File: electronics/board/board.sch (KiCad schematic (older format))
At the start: 50 parts

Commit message: Board update
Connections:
- net +5V: now also U?.24 (AVCC), U?.42 (AREF), U?.44 (AVCC)
- net at U?.1 (I1): now also U?.31 (PC6); no longer U?.18 (PD0)
- net at U?.2 (I2): now also U?.32 (PC7); no longer U?.19 (PD1)
- net at U?.3 (I3): now also U?.18 (PD0); no longer U?.20 (PD2)
- net at U?.4 (I4): now also U?.19 (PD1); no longer U?.21 (PD3)
- net at U?.5 (I5): now also U?.20 (PD2); no longer U?.25 (PD4)
- net at U?.6 (I6): now also U?.21 (PD3); no longer U?.22 (PD5)
- net at U?.7 (I7): now also U?.25 (PD4); no longer U?.26 (PD6)
- net at U?.8 (I8): now also U?.22 (PD5); no longer U?.27 (PD7)
- net at U?.1 (I1): now also U?.26 (PD6); no longer U?.41 (PF0)
- net at U?.2 (I2): now also U?.27 (PD7); no longer U?.40 (PF1)
- net at U?.3 (I3): now also U?.41 (PF0); no longer U?.39 (PF4)
- net at U?.4 (I4): now also U?.40 (PF1); no longer U?.38 (PF5)
- net at U?.5 (I5): now also U?.39 (PF4); no longer U?.37 (PF6)
- net at U?.6 (I6): now also U?.38 (PF5); no longer U?.36 (PF7)
- net at U?.7 (I7): now also U?.37 (PF6); no longer U?.31 (PC6)
- net at U?.8 (I8): now also U?.36 (PF7); no longer U?.32 (PC7)
- net at U?.2 (~RE): now also U?.3 (DE); no longer U?.29 (PB5)
- net at U?.30 (PB6): no longer U?.3 (DE)
- net at J?.1 (Pin_1), J?.1 (Pin_1), U?.6 (A): no longer U?.7 (B)
- net at J?.2 (Pin_2), J?.2 (Pin_2): now also U?.7 (B)
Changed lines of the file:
@@
 	10650 1150 10550 1150
 Wire Wire Line
-	1000 1450 9400 1450
-Wire Wire Line
-	10650 1550 1000 1550
+	10650 1550 9500 1550
 $Comp
 L pspice:DIODE D?
@@
 $EndComp
 Wire Wire Line
-	9050 2150 9400 2150
-Wire Wire Line
-	9400 2150 9400 1450
-Connection ~ 9400 1450
-Wire Wire Line
-	9400 1450 9550 1450
-Wire Wire Line
 	9550 1450 9550 2450
 Wire Wire Line
@@
 $EndComp
 Wire Wire Line
-	6200 3900 7550 3900
-Wire Wire Line
-	7550 3900 7550 3350
-Wire Wire Line
-	7550 3350 8250 3350
-Wire Wire Line
-	6200 4000 7600 4000
-Wire Wire Line
-	7600 4000 7600 3450
-Wire Wire Line
-	7600 3450 8250 3450
-Wire Wire Line
-	6200 4100 7650 4100
-Wire Wire Line
-	7650 4100 7650 3550
-Wire Wire Line
-	7650 3550 8250 3550
-Wire Wire Line
-	6200 4200 7700 4200
-Wire Wire Line
-	7700 4200 7700 3650
-Wire Wire Line
-	7700 3650 8250 3650
-Wire Wire Line
-	6200 4300 7750 4300
-Wire Wire Line
-	7750 4300 7750 3750
-Wire Wire Line
-	7750 3750 8250 3750
-Wire Wire Line
-	6200 4400 7800 4400
-Wire Wire Line
-	7800 4400 7800 3850
-Wire Wire Line
-	7800 3850 8250 3850
-Wire Wire Line
-	6200 4500 7850 4500
-Wire Wire Line
-	7850 4500 7850 3950
-Wire Wire Line
-	7850 3950 8250 3950
-Wire Wire Line
-	6200 4600 7900 4600
-Wire Wire Line
-	7900 4600 7900 4050
-Wire Wire Line
-	7900 4050 8250 4050
-Wire Wire Line
-	6200 5100 7600 5100
-Wire Wire Line
-	7600 5100 7600 4900
-Wire Wire Line
-	7600 4900 8300 4900
-Wire Wire Line
-	6200 5200 7650 5200
-Wire Wire Line
-	7650 5200 7650 5000
-Wire Wire Line
-	7650 5000 8300 5000
-Wire Wire Line
-	6200 5300 7700 5300
-Wire Wire Line
-	7700 5300 7700 5100
-Wire Wire Line
-	7700 5100 8300 5100
-Wire Wire Line
-	6200 5400 7750 5400
-Wire Wire Line
-	7750 5400 7750 5200
-Wire Wire Line
-	7750 5200 8300 5200
-Wire Wire Line
-	6200 5500 7800 5500
-Wire Wire Line
-	7800 5500 7800 5300
-Wire Wire Line
-	7800 5300 8300 5300
-Wire Wire Line
 	6200 3400 7050 3400
 Wire Wire Line
@@
 	8200 2450 8250 2450
 Wire Wire Line
-	6200 3300 7000 3300
-Wire Wire Line
-	7000 3300 7000 3200
-Wire Wire Line
-	8150 3200 8150 2350
-Wire Wire Line
-	8150 2350 8250 2350
-Wire Wire Line
-	6200 3200 6950 3200
-Wire Wire Line
-	6950 3200 6950 3150
-Wire Wire Line
-	6950 3150 8100 3150
-Wire Wire Line
-	8100 3150 8100 2250
-Wire Wire Line
-	8100 2250 8250 2250
-Wire Wire Line
 	6200 3100 8050 3100
 Wire Wire Line
@@
 Wire Wire Line
 	8050 2150 8250 2150
-Wire Wire Line
-	8300 5400 7850 5400
-Wire Wire Line
-	7850 5400 7850 5600
-Wire Wire Line
-	7850 5600 6200 5600
-Wire Wire Line
-	6200 3600 7050 3600
-Wire Wire Line
-	7050 3600 7050 5700
-Wire Wire Line
-	7050 5700 7900 5700
-Wire Wire Line
-	7900 5700 7900 5500
-Wire Wire Line
-	7900 5500 8300 5500
-Wire Wire Line
-	6200 3700 7000 3700
-Wire Wire Line
-	7000 3700 7000 5750
-Wire Wire Line
-	7000 5750 7950 5750
-Wire Wire Line
-	7950 5750 7950 5600
-Wire Wire Line
-	7950 5600 8300 5600
 $Comp
 L Amplifier_Operational:LMV358 U?
@@
 Text Notes 10700 1800 0    50   ~ 0
 RS485 BUS
-Wire Wire Line
-	7000 3200 8150 3200
 $Comp
 L Device:C C?
@@
 NoConn ~ 6200 2700
 NoConn ~ 6200 4900
+Wire Wire Line
+	1000 1450 9550 1450
+Wire Wire Line
+	9050 2150 9500 2150
+Wire Wire Line
+	9500 2150 9500 1550
+Connection ~ 9500 1550
+Wire Wire Line
+	9500 1550 1000 1550
+$Comp
+L power:+5V #PWR?
+U 1 1 5C1C840B
+P 5700 2100
+F 0 "#PWR?" H 5700 1950 50  0001 C CNN
+F 1 "+5V" H 5715 2273 50  0000 C CNN
+F 2 "" H 5700 2100 50  0001 C CNN
+F 3 "" H 5700 2100 50  0001 C CNN
+	1    5700 2100
+	1    0    0    -1
+$EndComp
+Wire Wire Line
+	5700 2100 5700 2400
+$Comp
+L power:+5V #PWR?
+U 1 1 5C1D6D5C
+P 4900 3300
+F 0 "#PWR?" H 4900 3150 50  0001 C CNN
+F 1 "+5V" H 4915 3473 50  0000 C CNN
+F 2 "" H 4900 3300 50  0001 C CNN
+F 3 "" H 4900 3300 50  0001 C CNN
+	1    4900 3300
+	1    0    0    -1
+$EndComp
+Wire Wire Line
+	4900 3300 5000 3300
+Wire Wire Line
+	8250 2350 8150 2350
+Wire Wire Line
+	8150 2350 8150 2250
+Wire Wire Line
+	8150 2250 8250 2250
+Wire Wire Line
+	6200 5600 8300 5600
+Wire Wire Line
+	6200 5500 8300 5500
+Wire Wire Line
+	6200 5400 8300 5400
+Wire Wire Line
+	6200 5300 8300 5300
+Wire Wire Line
+	6200 5200 8300 5200
+Wire Wire Line
+	6200 5100 8300 5100
+Wire Wire Line
+	6200 4600 7600 4600
+Wire Wire Line
+	7600 4600 7600 5000
+Wire Wire Line
+	7600 5000 8300 5000
+Wire Wire Line
+	6200 4500 7700 4500
+Wire Wire Line
+	7700 4500 7700 4900
+Wire Wire Line
+	7700 4900 8300 4900
+Wire Wire Line
+	6200 4400 8250 4400
+Wire Wire Line
+	8250 4400 8250 4050
+Wire Wire Line
+	6200 4300 8200 4300
+Wire Wire Line
+	8200 4300 8200 3950
+Wire Wire Line
+	8200 3950 8250 3950
+Wire Wire Line
+	6200 4200 8150 4200
+Wire Wire Line
+	8150 4200 8150 3850
+Wire Wire Line
+	8150 3850 8250 3850
+Wire Wire Line
+	6200 4100 8100 4100
+Wire Wire Line
+	8100 4100 8100 3750
+Wire Wire Line
+	8100 3750 8250 3750
+Wire Wire Line
+	6200 4000 8050 4000
+Wire Wire Line
+	8050 4000 8050 3650
+Wire Wire Line
+	8050 3650 8250 3650
+Wire Wire Line
+	6200 3900 8000 3900
+Wire Wire Line
+	8000 3900 8000 3550
+Wire Wire Line
+	8000 3550 8250 3550
+Wire Wire Line
+	6200 3700 7950 3700
+Wire Wire Line
+	7950 3450 8250 3450
+Wire Wire Line
+	7950 3450 7950 3700
+Wire Wire Line
+	6200 3600 7900 3600
+Wire Wire Line
+	7900 3600 7900 3350
+Wire Wire Line
+	7900 3350 8250 3350
 $EndSCHEMATC

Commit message: Board annotation
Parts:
- added SW1: SW_Push_Open_Dual, symbol Switch:SW_Push_Open_Dual
- gave numbers to parts that had none: 50
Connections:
- net GND: now also SW1.1, SW1.3
- net RESET: now also SW1.2, SW1.4
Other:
- note added: "Power on reset + reset switch"
- note removed: "USB Autoreset\nTODO: risk of RESET or oRESET inverted here?"
- moved on the sheet: C7, D1, R3

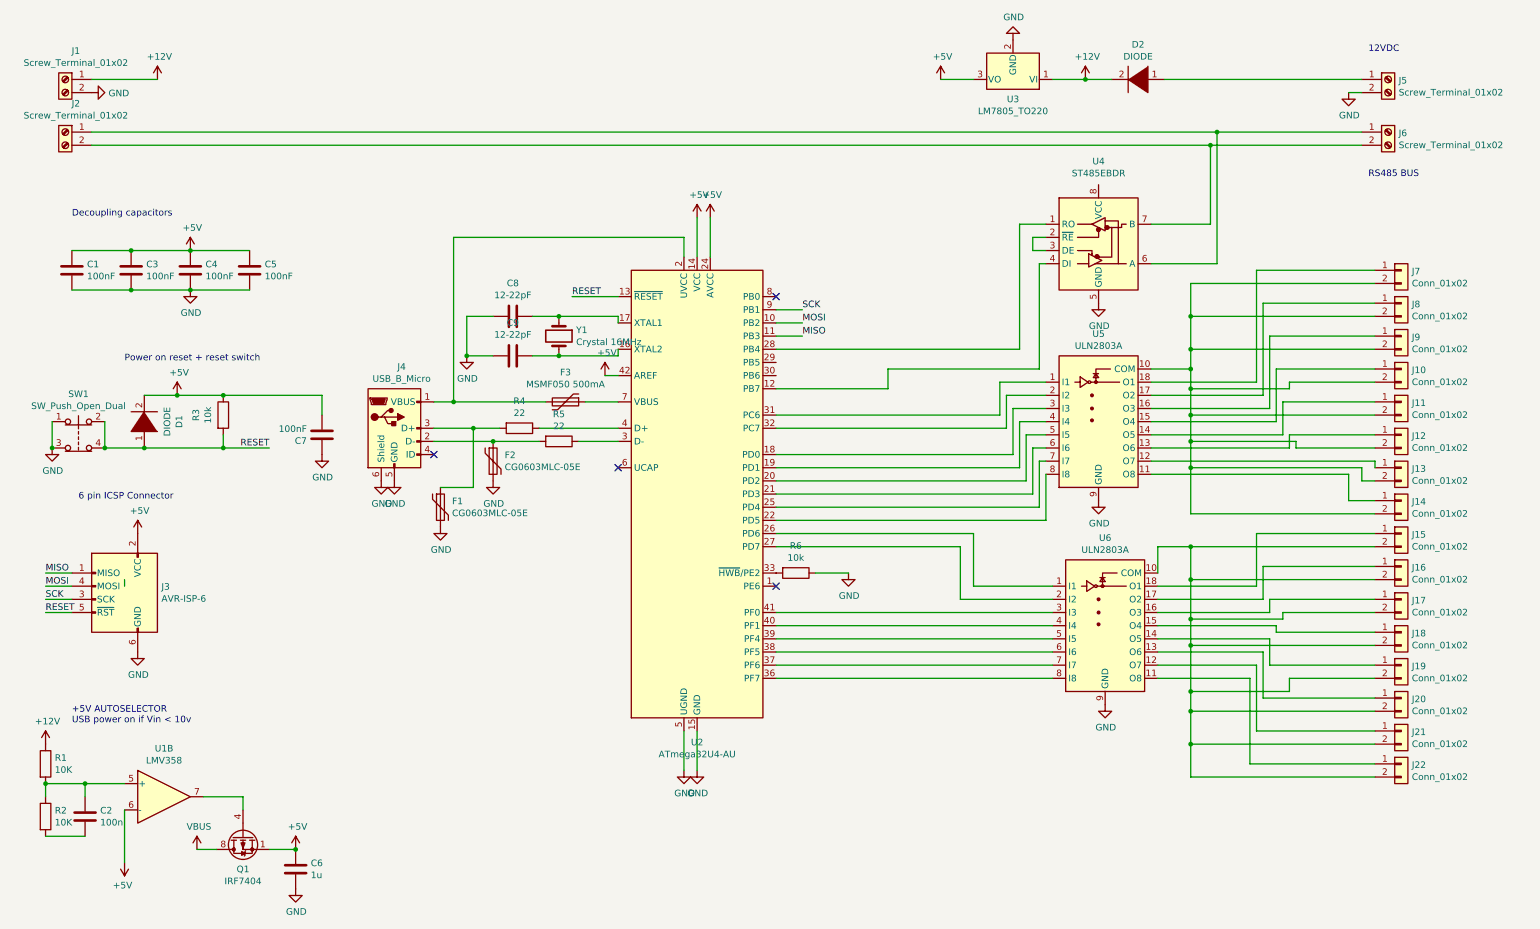
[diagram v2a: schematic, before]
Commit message: Footprints and models
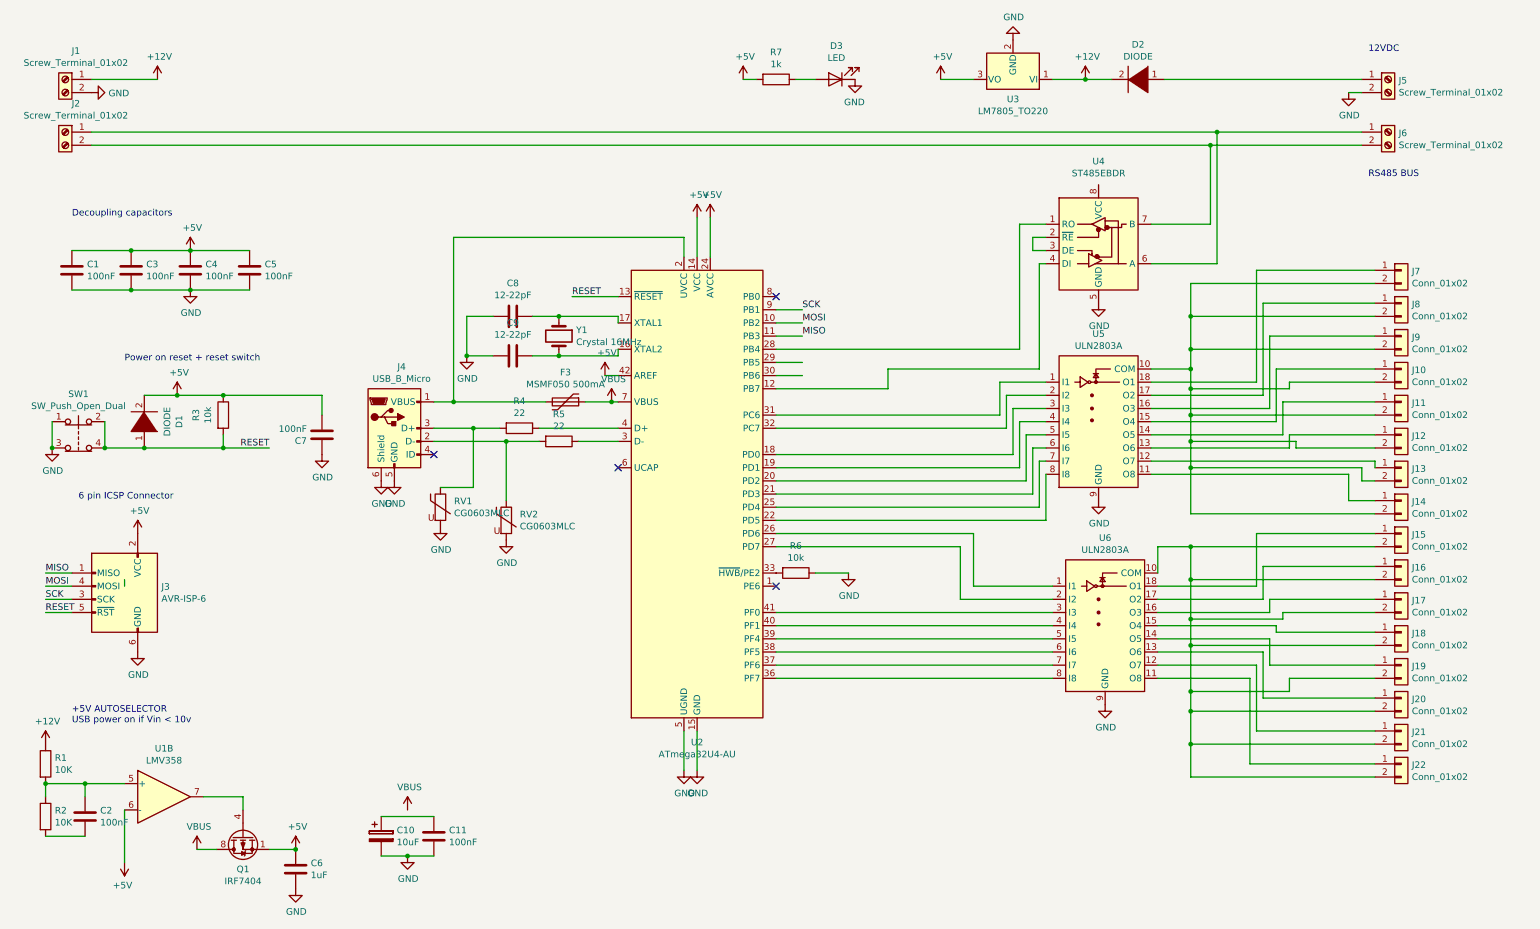
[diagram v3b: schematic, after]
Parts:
- removed F1, F2: CG0603MLC-05E, symbol Device:Polyfuse
- added C10: 10uF, Capacitor_SMD:CP_Elec_6.3x5.2, symbol Device:CP
- added C11: 100nF, Capacitor_SMD:C_0603_1608Metric, symbol Device:C
- added D3: LED, LED_SMD:LED_0805_2012Metric, symbol Device:LED
- added R7: 1k, Resistor_SMD:R_0603_1608Metric, symbol Device:R
- added RV1, RV2: CG0603MLC, Resistor_SMD:R_0603_1608Metric, symbol Device:Varistor
- C1, C3, C4, C5, C7, C8, C9: footprint (none) -> Capacitor_SMD:C_0603_1608Metric
- C2: value 100n -> 100nF; footprint (none) -> Capacitor_SMD:C_0603_1608Metric
- C6: value 1u -> 1uF; footprint (none) -> Capacitor_SMD:C_0603_1608Metric
- D1: footprint (none) -> Diode_SMD:D_0603_1608Metric
- D2: footprint (none) -> Diode_SMD:D_1210_3225Metric
- F3: footprint (none) -> Fuse:Fuse_1812_4532Metric
- J1, J2, J5, J6: footprint (none) -> TerminalBlock_4Ucon:TerminalBlock_4Ucon_1x02_P3.50mm_Vertical
- J10, J11, J12, J13, J14, J15, J16, J17, J18, J19, J20, J21, J22, J7, J8, J9: footprint (none) -> Connector_JST:JST_ACH_BBM02B-ACHSS-GAN-ETF_1x02-1MP_P1.20mm_Vertical
- J3: footprint (none) -> Connector_PinHeader_2.54mm:PinHeader_2x03_P2.54mm_Vertical_SMD
- J4: footprint (none) -> Connector_USB:USB_Micro-B_Molex_47346-0001
- R1, R2, R3, R4, R5, R6: footprint (none) -> Resistor_SMD:R_0603_1608Metric
- SW1: footprint (none) -> Button_Switch_SMD:SW_SPST_PTS645
- U1: footprint (none) -> Package_SO:MSOP-8-1EP_3x3mm_P0.65mm_EP2.54x2.8mm_ThermalVias
- U5, U6: footprint (none) -> Package_SO:SOP-18_7.0x12.5mm_P1.27mm
- Y1: footprint (none) -> Crystal:Crystal_SMD_SeikoEpson_MC405-2Pin_9.6x4.1mm
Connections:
- net +5V: now also R7.2
- net GND: now also C10.2, C11.2, D3.1 (K), RV1.2, RV2.2
- net VBUS: now also F3.1, U2.7 (VBUS)
- net at J4.2 (D-), R5.2: now also RV2.1
- net at J4.3 (D+), R4.2: now also RV1.1
- new net: C10.1, C11.1
- new net: D3.2 (A), R7.1
